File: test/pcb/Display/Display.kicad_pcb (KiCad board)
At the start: 2 copper layers, 36 x 26 mm, 15 parts, among them J1 Conn_01x10, J2 Conn_01x02, J3 Conn_01x02, U1 UG-2864ASWPG01

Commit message: Version 0.4.0
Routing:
- net +12V: track 14.6 -> 13.7 mm

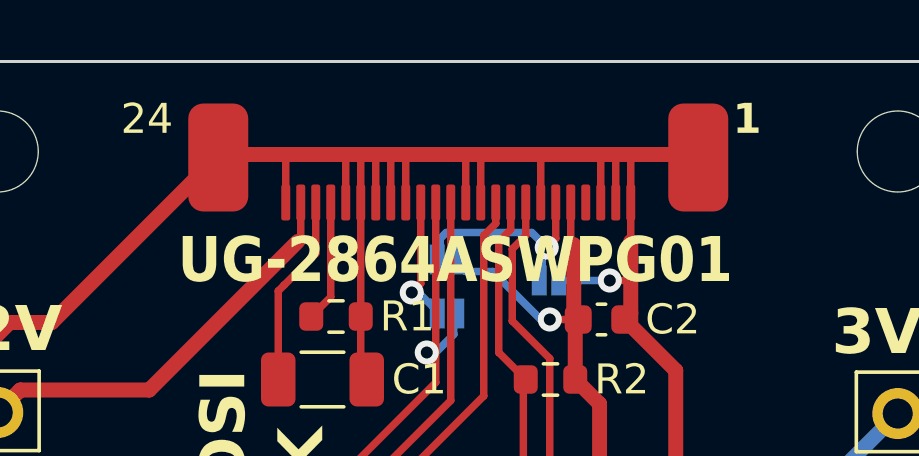
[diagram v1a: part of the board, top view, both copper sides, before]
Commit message: Use steps variable
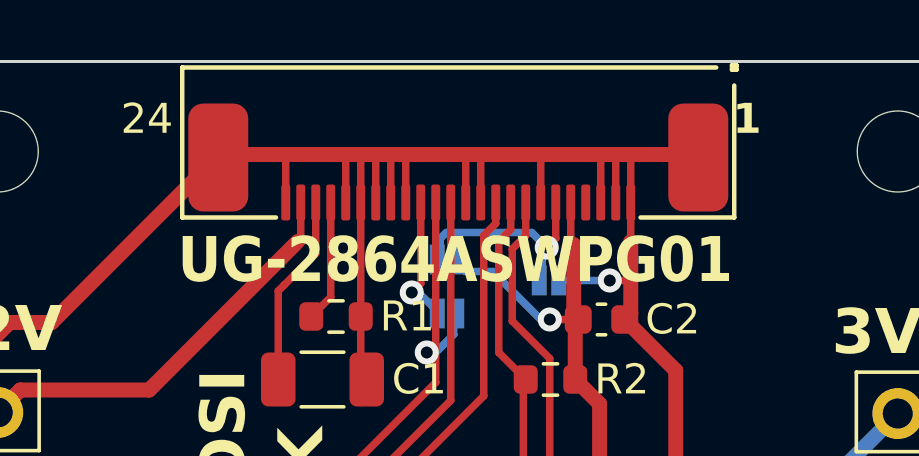
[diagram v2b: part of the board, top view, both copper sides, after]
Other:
- board text added: "${VERSION}"
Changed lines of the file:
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@@
 	)
 	(paper "A4")
+	(title_block
+		(title "Display Test")
+		(date "2026-02-27")
+		(rev "${VERSION}")
+	)
 	(layers
 		(0 "F.Cu" signal)
@@
 		)
 	)
+	(property "VERSION" "0.4.0")
 	(net 0 "")
 	(net 1 "Net-(U1-VCOMH)")
@@
 		(fp_line
 			(start 9.2 3)
+			(end 9.2 -2)
+			(stroke
+				(width 0.15)
+				(type solid)
+			)
+			(layer "F.SilkS")
+		)
+		(fp_line
+			(start 9.2 -2)
+			(end 6.075 -2)
+			(stroke
+				(width 0.15)
+				(type solid)
+			)
+			(layer "F.SilkS")
+		)
+		(fp_line
+			(start -6.075 -2)
+			(end -9.2 -2)
+			(stroke
+				(width 0.15)
+				(type solid)
+			)
+			(layer "F.SilkS")
+		)
+		(fp_line
+			(start -8.6 3)
+			(end 9.2 3)
+			(stroke
+				(width 0.15)
+				(type solid)
+			)
+			(layer "F.SilkS")
+		)
+		(fp_line
+			(start -9.125 3.075)
+			(end -9.275 3.075)
+			(stroke
+				(width 0.15)
+				(type solid)
+			)
+			(layer "F.SilkS")
+		)
+		(fp_line
+			(start -9.125 2.925)
+			(end -9.125 3.075)
+			(stroke
+				(width 0.15)
+				(type solid)
+			)
+			(layer "F.SilkS")
+		)
+		(fp_line
+			(start -9.2 -2)
+			(end -9.2 2.4)
+			(stroke
+				(width 0.15)
+				(type solid)
+			)
+			(layer "F.SilkS")
+		)
+		(fp_line
+			(start -9.275 3.075)
+			(end -9.275 2.925)
+			(stroke
+				(width 0.15)
+				(type solid)
+			)
+			(layer "F.SilkS")
+		)
+		(fp_line
+			(start -9.275 2.925)
+			(end -9.125 2.925)
+			(stroke
+				(width 0.15)
+				(type solid)
+			)
+			(layer "F.SilkS")
+		)
+		(fp_line
+			(start 9.2 3)
 			(end -9.2 3)
 			(stroke
@@
 		)
 		(fp_line
-			(start 9.2 -3)
+			(start 9.2 -2)
 			(end 9.2 3)
 			(stroke
@@
 		(fp_line
 			(start -9.2 3)
-			(end -9.2 -3)
-			(stroke
-				(width 0.05)
-				(type solid)
-			)
-			(layer "F.CrtYd")
-		)
-		(fp_line
-			(start -9.2 -3)
-			(end 9.2 -3)
+			(end -9.2 -2)
+			(stroke
+				(width 0.05)
+				(type solid)
+			)
+			(layer "F.CrtYd")
+		)
+		(fp_line
+			(start -9.2 -2)
+			(end 9.2 -2)
 			(stroke
 				(width 0.05)
@@
 		(fp_line
 			(start 9.2 3)
-			(end 9.2 -3)
+			(end 9.2 -2)
 			(stroke
 				(width 0.15)
@@
 		)
 		(fp_line
-			(start 9.2 -3)
-			(end -9.2 -3)
+			(start 9.2 -2)
+			(end -9.2 -2)
 			(stroke
 				(width 0.15)
@@
 		)
 		(fp_line
-			(start -7.7 3)
+			(start -7.95 3)
 			(end 9.2 3)
 			(stroke
@@
 		)
 		(fp_line
-			(start -7.7 3)
-			(end -9.2 1.5)
+			(start -7.95 3)
+			(end -9.2 1.75)
 			(stroke
 				(width 0.15)
@@
 		)
 		(fp_line
-			(start -9.2 -3)
-			(end -9.2 1.5)
+			(start -9.2 -2)
+			(end -9.2 1.75)
 			(stroke
 				(width 0.15)
@@
 		(layer "B.SilkS")
 	)
+	(gr_line
+		(start 150.925 92.025)
+		(end 148.175 92.025)
+		(stroke
+			(width 0.15)
+			(type default)
+		)
+		(layer "Cmts.User")
+	)
 	(gr_rect
 		(start 122 87)
@@
 				(bold yes)
 			)
+			(justify left bottom mirror)
+		)
+	)
+	(gr_text "${VERSION}"
+		(at 143.375 89.35 0)
+		(layer "B.SilkS")
+		(effects
+			(font
+				(size 1.5 1.5)
+				(thickness 0.3)
+				(bold yes)
+			)

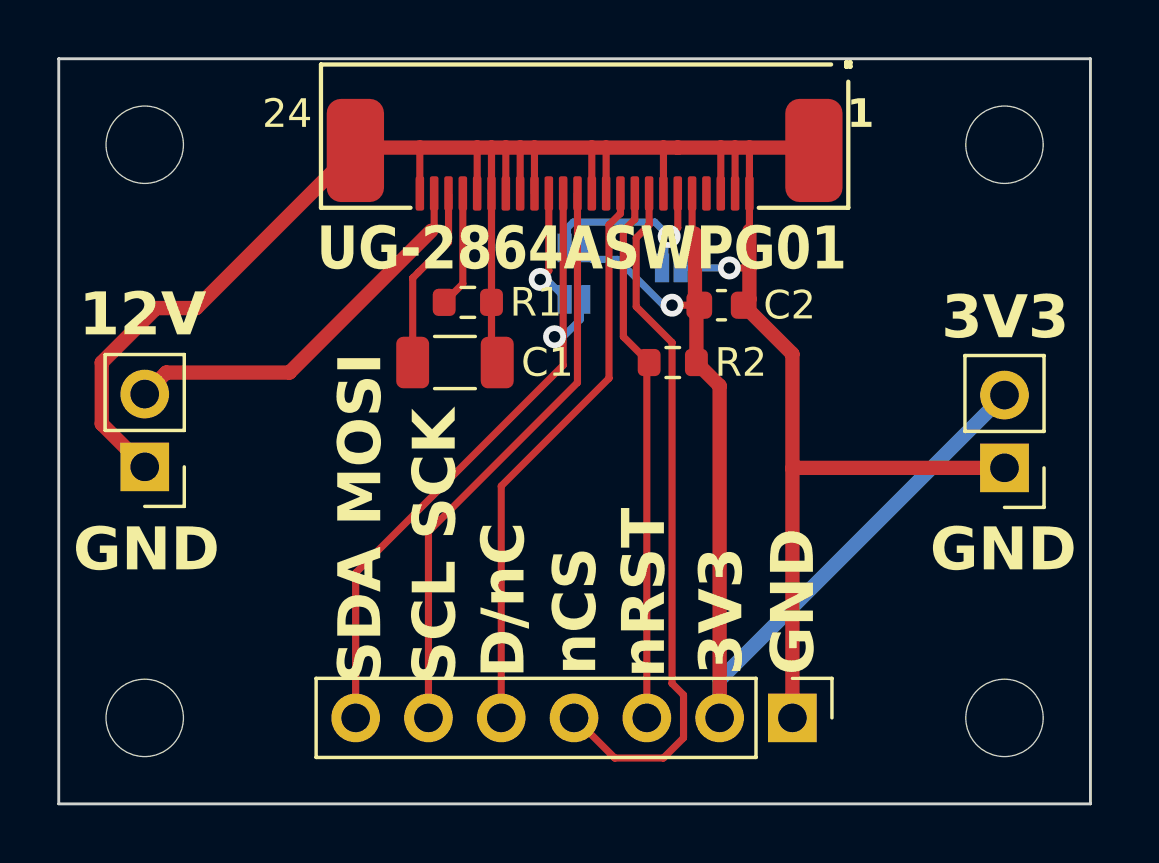
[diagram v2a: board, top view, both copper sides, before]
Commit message: Rename test/LedControl to test/LedControl-g431
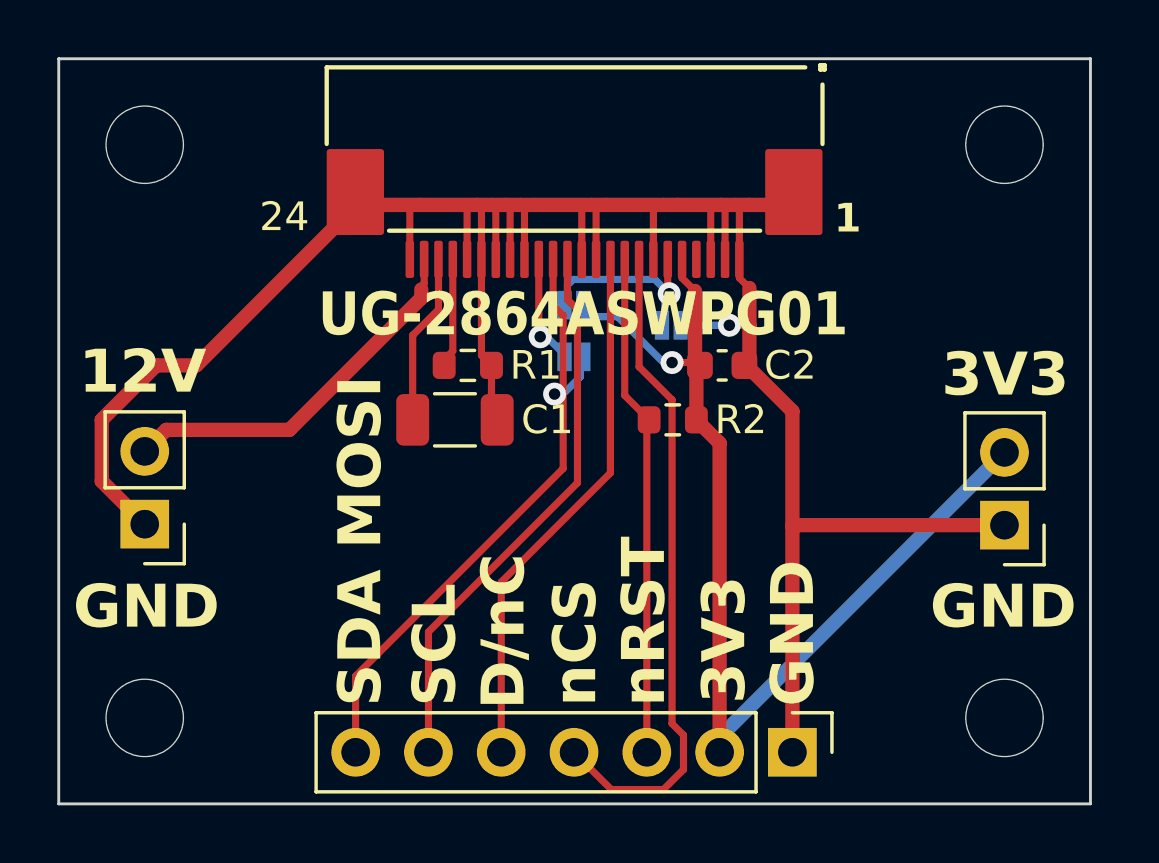
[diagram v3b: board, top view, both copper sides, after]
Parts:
- U1: footprint local:Connector-Flat-24_P0.5mm -> local:Connector-Flat-24-0.5mm
- moved U1 2.72 mm to (140.0, 92.9)
- moved R1 2.20 mm to (136.3, 97.7)
- moved C2 2.10 mm to (145.2, 97.7)
- moved C1 2.00 mm to (135.8, 99.6)
- moved J2 2.00 mm to (125.0, 103.2)
- moved J3 2.00 mm to (155.0, 103.3)
- moved JP1 2.00 mm to (140.0, 95.6)
- moved JP2 2.00 mm to (140.0, 97.4)
- moved JP3 2.00 mm to (143.4, 96.3)
- moved R2 2.00 mm to (143.4, 99.6)
- moved J1 1.20 mm to (147.6, 111.2)
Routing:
- net +3V3: track 39.0 -> 37.2 mm
- net nCS: track 24.6 -> 23.1 mm
- net nRST: track 18.9 -> 17.6 mm
- net D/nC: track 20.0 -> 18.8 mm
- net SDA_MOSI: track 23.3 -> 22.3 mm
- net SCL_SCK: track 20.5 -> 19.5 mm
- net GND: track 86.7 -> 86.2 mm
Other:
- board text added: "SCK"
- board text added: "SCL"
- board text removed: "SCL SCK"
